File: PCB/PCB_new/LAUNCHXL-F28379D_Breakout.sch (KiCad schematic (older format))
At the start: 21 parts, among them IC1 LM358N, Q1 100V/17A, Q2 100V/17A, Q3 100V/17A, Q4 100V/17A, Q5 100V/17A, Q6 100V/17A

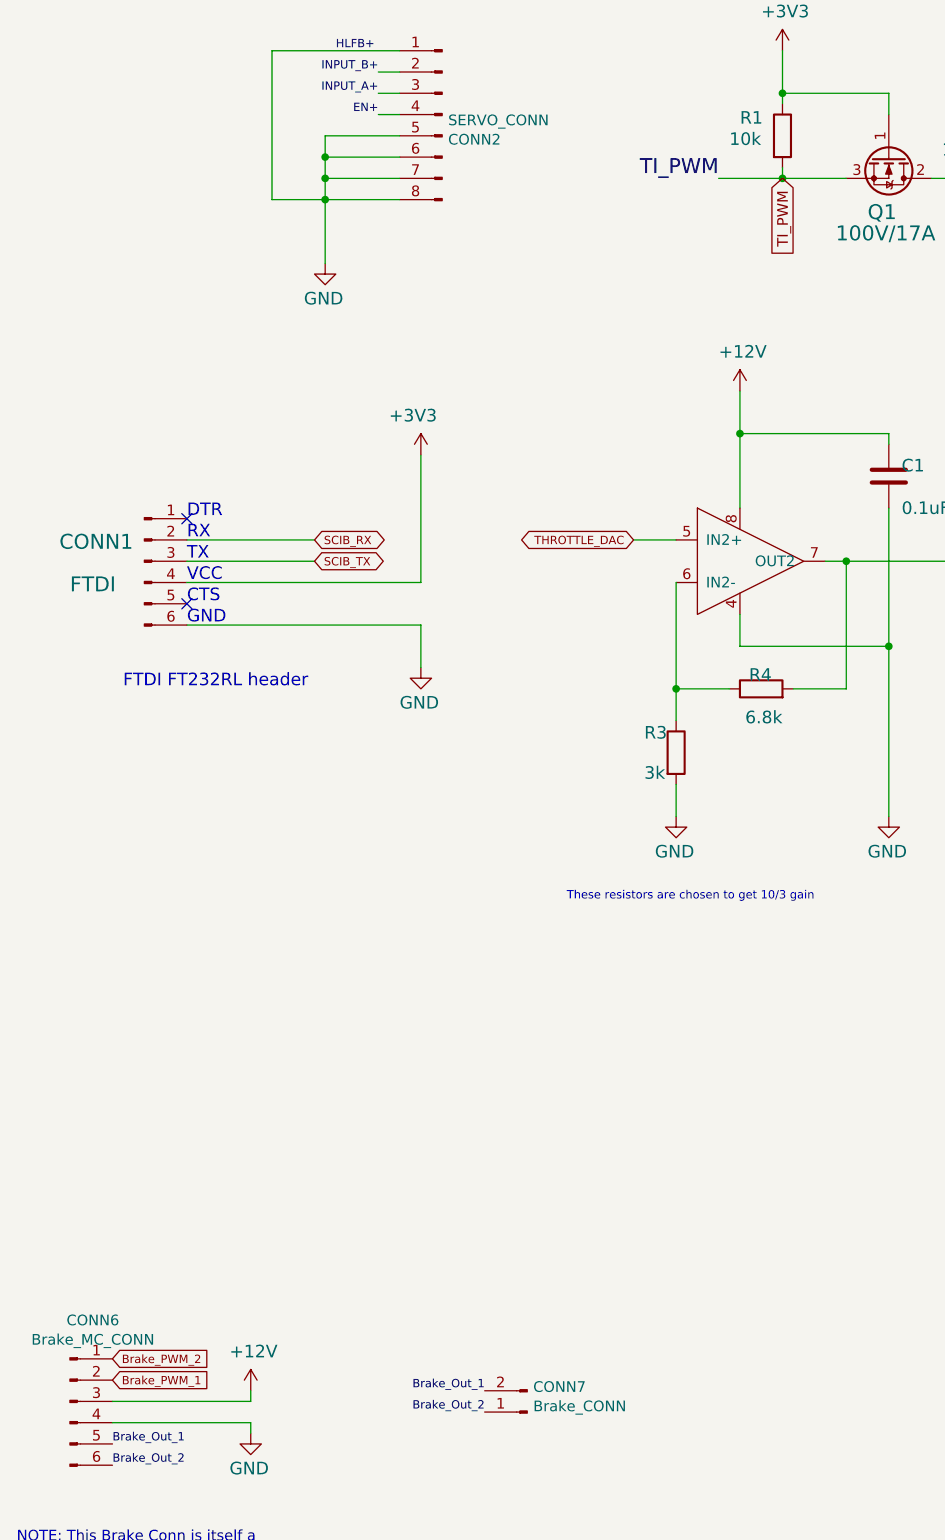
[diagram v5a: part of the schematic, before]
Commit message: changed board to work with arduino due
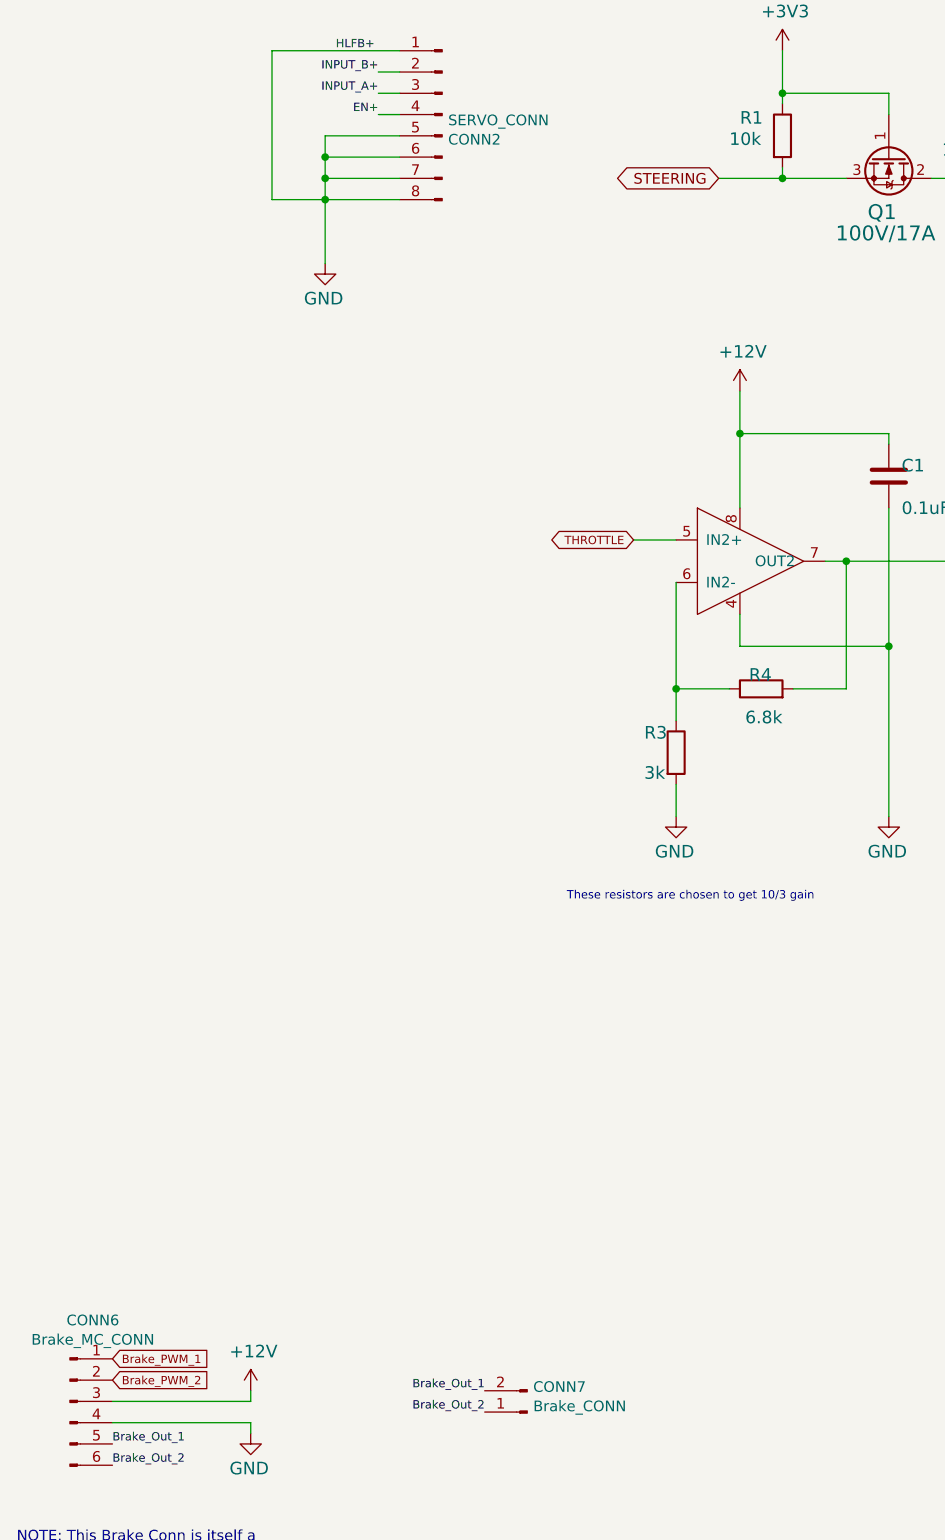
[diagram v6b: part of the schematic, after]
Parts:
- removed FTDI: FTDI, Drivetrain_control:FTDI_CONN, symbol Connector:Conn_01x06_Male
- CONN6: footprint Drivetrain_control:Brake_MC_Conn_6pin -> Drivetrain_control:Brake_MC_Conn_6_pin
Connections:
- net Brake_PWM_1: now also CONN6.1 (Pin_1); no longer CONN6.2 (Pin_2)
- net Brake_PWM_2: now also CONN6.2 (Pin_2); no longer CONN6.1 (Pin_1)
- net THROTTLE_DAC renamed THROTTLE
- net TI_PWM renamed STEERING
- no-connect marks 2 -> 0
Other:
- note removed: "CTS"
- note removed: "DTR"
- note removed: "FTDI FT232RL header"
- note removed: "GND"
- note removed: "RX"
- note removed: "TX"
- note removed: "VCC"
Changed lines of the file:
@@
 $EndDescr
-Wire Wire Line
-	2000 3800 3100 3800
-Wire Wire Line
-	3100 3800 3100 4000
 Wire Wire Line
 	4600 3900 5300 3900
@@
 	4300 3600 4300 4100
 Connection ~ 4300 4100
-Text GLabel 4100 3400 0    39   BiDi ~ 0
-THROTTLE_DAC
-Wire Wire Line
-	2000 3400 2600 3400
-Text GLabel 2600 3400 2    39   BiDi ~ 0
-SCIB_RX
-Wire Wire Line
-	2000 3500 2600 3500
-Text GLabel 2600 3500 2    39   BiDi ~ 0
-SCIB_TX
-Wire Wire Line
-	2000 3600 3100 3600
-Wire Wire Line
-	3100 3600 3100 3000
 Wire Wire Line
 	4800 1300 4800 1100
@@
 Text Label 10950 4550 2    39   ~ 0
 REV_MC
-Text Label 4500 1700 2    70   ~ 0
-TI_PWM
 Wire Wire Line
 	10300 1500 10200 1500
@@
 $EndComp
 $Comp
-L power:+3V3 #+3V1
-U 1 1 612E3AAF
-P 3100 3000
-AR Path="/612E3AAF" Ref="#+3V1"  Part="1"
-AR Path="/5DD5E236/612E3AAF" Ref="#+3V1"  Part="1"
-AR Path="/5DF27AC1/612E3AAF" Ref="#+3V01"  Part="1"
-F 0 "#+3V01" H 3100 3000 50  0001 C CNN
-F 1 "+3V3" H 2950 3150 59  0000 L BNN
-F 2 "" H 3100 3000 50  0001 C CNN
-F 3 "" H 3100 3000 50  0001 C CNN
-	1    3100 3000
-	1    0    0    -1
-$EndComp
-$Comp
-L power:GND #GND1
-U 1 1 A7315E89
-P 3100 4000
-AR Path="/A7315E89" Ref="#GND1"  Part="1"
-AR Path="/5DD5E236/A7315E89" Ref="#GND1"  Part="1"
-AR Path="/5DF27AC1/A7315E89" Ref="#GND01"  Part="1"
-F 0 "#GND01" H 3100 4000 50  0001 C CNN
-F 1 "GND" H 3000 3800 59  0000 L BNN
-F 2 "" H 3100 4000 50  0001 C CNN
-F 3 "" H 3100 4000 50  0001 C CNN
-	1    3100 4000
-	1    0    0    -1
-$EndComp
-$Comp
 L power:+12V #P+1
 U 1 1 48DD0DF0
@@
 	1    0    0    -1
 $EndComp
-Text Notes 2000 3600 0    59   ~ 0
-VCC
-Text Notes 2000 3500 0    59   ~ 0
-TX
-Text Notes 2000 3400 0    59   ~ 0
-RX
-Text Notes 2000 3300 0    59   ~ 0
-DTR
-Text Notes 2000 3700 0    59   ~ 0
-CTS
-Text Notes 2000 3800 0    59   ~ 0
-GND
-Text Notes 1700 4100 0    59   ~ 0
-FTDI FT232RL header
 Text Notes 7200 900  0    59   ~ 0
 12V supply comes from DC-DC Converter\nwhich supplies 13.8 nominal and 12V @ peak current
-Text GLabel 4800 1700 3    50   Input ~ 0
-TI_PWM
+Text GLabel 4500 1700 0    50   BiDi ~ 0
+STEERING
 Wire Wire Line
 	5500 1700 5800 1700
@@
 Wire Wire Line
 	2650 1800 2650 2100
-NoConn ~ 2000 3300
-NoConn ~ 2000 3700
 $Comp
 L Connector:Conn_01x08_Male CONN2
@@
 $EndComp
 $Comp
-L Connector:Conn_01x06_Male FTDI
-U 1 1 A664394C
-P 1800 3500
-AR Path="/A664394C" Ref="FTDI"  Part="1"
-AR Path="/5DD5E236/A664394C" Ref="FTDI"  Part="1"
-AR Path="/5DF27AC1/A664394C" Ref="CONN1"  Part="1"
-F 0 "CONN1" H 1400 3550 70  0000 L BNN
-F 1 "FTDI" H 1450 3350 70  0000 L BNN
-F 2 "Drivetrain_control:FTDI_CONN" H 1800 3500 50  0001 C CNN
-F 3 "https://www.digikey.com/product-detail/en/sparkfun-electronics/BOB-13263/1568-1720-ND/7675364?utm_adgroup=DEV+Boards&utm_source=google&utm_medium=cpc&utm_campaign=Shopping_Development%20Boards%2C%20Kits%2C%20Programmers&utm_term=&utm_content=DEV+Boards&gclid=CjwKCAiA3uDwBRBFEiwA1VsajG8ZEU__rDO9vt75xZ_ZmVJpdzuR2nNYhmOuDHuQax7VeKlEBKAZyxoCcLwQAvD_BwE" H 1800 3500 50  0001 C CNN
-	1    1800 3500
-	1    0    0    -1
-$EndComp
-$Comp
 L Device:Q_NMOS_GDS Q?
 U 1 1 5E16D782
@@
 F 0 "CONN6" H 1558 7831 50  0000 C CNN
 F 1 "Brake_MC_CONN" H 1558 7740 50  0000 C CNN
-F 2 "Drivetrain_control:Brake_MC_Conn_6pin" H 1450 7450 50  0001 C CNN
+F 2 "Drivetrain_control:Brake_MC_Conn_6_pin" H 1450 7450 50  0001 C CNN
 F 3 "https://cdn-shop.adafruit.com/product-files/3190/drv8871.pdf" H 1450 7450 50  0001 C CNN
 F 4 "https://learn.adafruit.com/adafruit-drv8871-brushed-dc-motor-driver-breakout/" H 1450 7450 50  0001 C CNN "Website"
@@
 	1    0    0    -1
 $EndComp
+Text GLabel 1650 7350 2    39   Input ~ 0
+Brake_PWM_2
 Text GLabel 1650 7250 2    39   Input ~ 0
-Brake_PWM_2
-Text GLabel 1650 7350 2    39   Input ~ 0
 Brake_PWM_1
 $Comp
@@
 	0    1    1    0
 $EndComp
+Text GLabel 4100 3400 0    39   BiDi ~ 0
+THROTTLE
 $EndSCHEMATC
